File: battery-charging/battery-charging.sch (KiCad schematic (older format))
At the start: 20 parts, among them J101 USB_B_Micro, J102 BAT-, J103 BAT+, U101 TC4056A, U102 MT3608

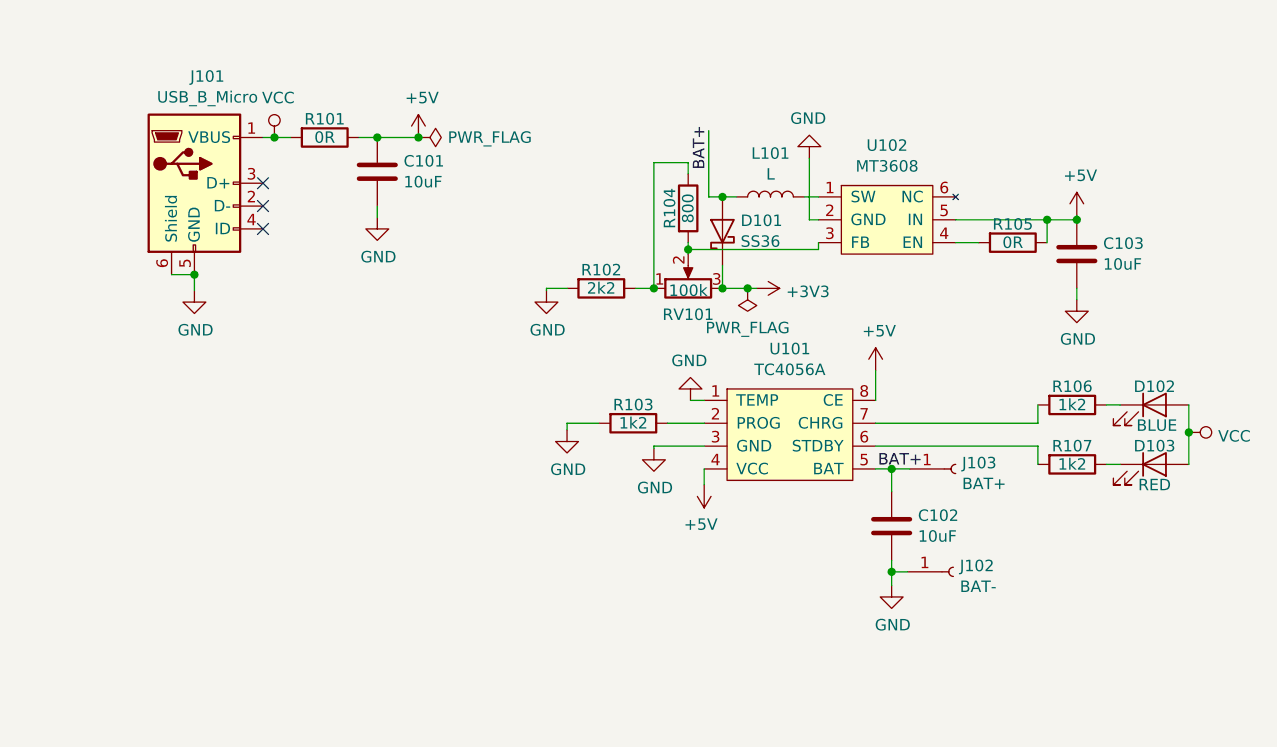
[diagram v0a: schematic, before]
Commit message: added C167321 usb c
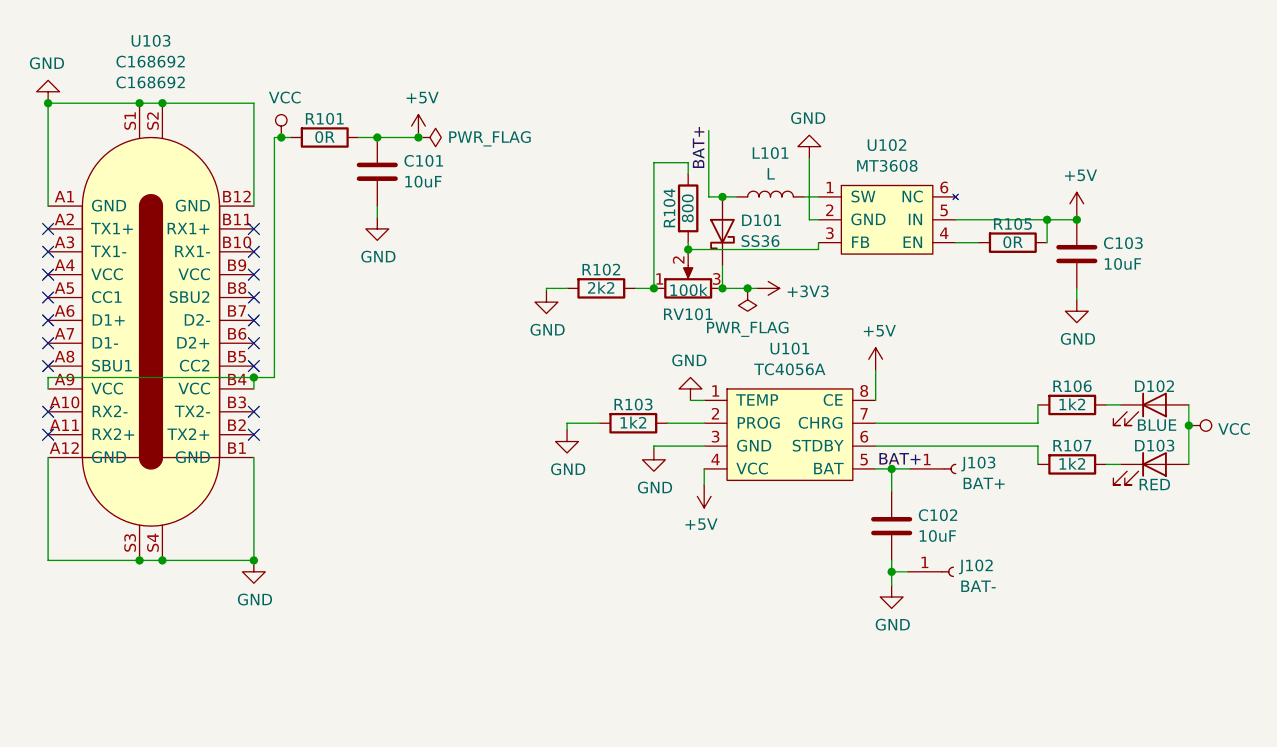
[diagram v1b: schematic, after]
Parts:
- removed J101: USB_B_Micro, Connector_USB:USB_Micro-B_Molex_47346-0001, symbol Connector:USB_B_Micro
- added U103: C168692, water-lib:C168692, symbol water-lib:C168692
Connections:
- net GND: now also U103.A1 (GND), U103.A12 (GND), U103.B1 (GND), U103.B12 (GND), U103.S1, U103.S2, U103.S3, U103.S4
- net VCC: now also U103.A9 (VCC), U103.B4 (VCC)
- no-connect marks 3 -> 18
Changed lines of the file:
@@
 EESchema Schematic File Version 4
+LIBS:battery-charging-cache
 EELAYER 30 0
 EELAYER END
@@
 $EndDescr
 $Comp
-L Connector:USB_B_Micro J101
-U 1 1 5DB449B5
-P 1580 1770
-F 0 "J101" H 1637 2237 50  0000 C CNN
-F 1 "USB_B_Micro" H 1637 2146 50  0000 C CNN
-F 2 "Connector_USB:USB_Micro-B_Molex_47346-0001" H 1730 1720 50  0001 C CNN
-F 3 "~" H 1730 1720 50  0001 C CNN
-	1    1580 1770
-	1    0    0    -1
-$EndComp
-$Comp
 L battery:TC4056A U101
 U 1 1 5DB4BCFC
@@
 	1    0    0    -1
 $EndComp
-NoConn ~ 1880 1770
-NoConn ~ 1880 1870
-Wire Wire Line
-	1480 2170 1580 2170
-Wire Wire Line
-	1580 2170 1580 2240
-Connection ~ 1580 2170
-$Comp
-L power:GND #PWR0101
-U 1 1 5DB4CB22
-P 1580 2240
-F 0 "#PWR0101" H 1580 1990 50  0001 C CNN
-F 1 "GND" H 1585 2067 50  0000 C CNN
-F 2 "" H 1580 2240 50  0001 C CNN
-F 3 "" H 1580 2240 50  0001 C CNN
-	1    1580 2240
-	1    0    0    -1
-$EndComp
 $Comp
 L Device:R R101
@@
 	0    1    1    0
 $EndComp
-Wire Wire Line
-	1880 1570 1930 1570
 $Comp
 L Device:C C101
@@
 	1    0    0    -1
 $EndComp
-NoConn ~ 1880 1970
 $Comp
 L power:GND #PWR0103
@@
 L power:VCC #PWR0110
 U 1 1 5DB57939
-P 1930 1570
-F 0 "#PWR0110" H 1930 1420 50  0001 C CNN
-F 1 "VCC" H 1947 1743 50  0000 C CNN
-F 2 "" H 1930 1570 50  0001 C CNN
-F 3 "" H 1930 1570 50  0001 C CNN
-	1    1930 1570
-	1    0    0    -1
-$EndComp
-Connection ~ 1930 1570
-Wire Wire Line
-	1930 1570 2000 1570
+P 1960 1570
+F 0 "#PWR0110" H 1960 1420 50  0001 C CNN
+F 1 "VCC" H 1977 1743 50  0000 C CNN
+F 2 "" H 1960 1570 50  0001 C CNN
+F 3 "" H 1960 1570 50  0001 C CNN
+	1    1960 1570
+	1    0    0    -1
+$EndComp
+Wire Wire Line
+	1930 1570 1960 1570
 $Comp
 L power:VCC #PWR0111
 U 1 1 5DB58014
-P 5930 2860
-F 0 "#PWR0111" H 5930 2710 50  0001 C CNN
-F 1 "VCC" V 5947 2988 50  0000 L CNN
-F 2 "" H 5930 2860 50  0001 C CNN
-F 3 "" H 5930 2860 50  0001 C CNN
-	1    5930 2860
+P 5930 2830
+F 0 "#PWR0111" H 5930 2680 50  0001 C CNN
+F 1 "VCC" V 5947 2958 50  0000 L CNN
+F 2 "" H 5930 2830 50  0001 C CNN
+F 3 "" H 5930 2830 50  0001 C CNN
+	1    5930 2830
 	0    1    1    0
 $EndComp
@@
 	1    0    0    -1
 $EndComp
-Wire Wire Line
-	5930 2740 5930 2860
-Connection ~ 5930 2860
-Wire Wire Line
-	5930 2860 5930 3000
 Wire Wire Line
 	5630 2740 5570 2740
@@
 $EndComp
 Connection ~ 2560 1570
+$Comp
+L water-lib:C168692 U103
+U 1 1 5DEF8B80
+P 1390 2370
+F 0 "U103" H 1390 3591 50  0000 C CNN
+F 1 "C168692" H 1390 3500 50  0000 C CNN
+F 2 "water-lib:C168692" H 1240 2370 50  0001 C CNN
+F 3 "https://datasheet.lcsc.com/szlcsc/1811141426_Jing-Extension-of-the-Electronic-Co-C168692_C168692.pdf" H 1240 2370 50  0001 C CNN
+F 4 "C168692" H 1390 3409 50  0000 C CNN "LCSC"
+	1    1390 2370
+	1    0    0    -1
+$EndComp
+Wire Wire Line
+	940  1870 940  1420
+Wire Wire Line
+	940  1420 1340 1420
+Wire Wire Line
+	1840 1420 1840 1870
+Connection ~ 1340 1420
+Wire Wire Line
+	1340 1420 1440 1420
+Connection ~ 1440 1420
+Wire Wire Line
+	1440 1420 1840 1420
+Wire Wire Line
+	940  2670 940  2620
+Wire Wire Line
+	940  2620 1840 2620
+Wire Wire Line
+	1840 2620 1840 2670
+Wire Wire Line
+	1930 1570 1930 2620
+Wire Wire Line
+	1930 2620 1840 2620
+Connection ~ 1840 2620
+Wire Wire Line
+	940  2970 940  3420
+Wire Wire Line
+	940  3420 1340 3420
+Wire Wire Line
+	1840 3420 1840 2970
+Connection ~ 1340 3420
+Wire Wire Line
+	1340 3420 1440 3420
+Connection ~ 1440 3420
+Wire Wire Line
+	1440 3420 1840 3420
+NoConn ~ 940  1970
+NoConn ~ 940  2070
+NoConn ~ 940  2170
+NoConn ~ 940  2270
+NoConn ~ 940  2370
+NoConn ~ 940  2470
+NoConn ~ 940  2570
+NoConn ~ 940  2770
+NoConn ~ 940  2870
+NoConn ~ 1840 2870
+NoConn ~ 1840 2770
+NoConn ~ 1840 2570
+NoConn ~ 1840 2470
+NoConn ~ 1840 2370
+NoConn ~ 1840 2270
+NoConn ~ 1840 2170
+NoConn ~ 1840 2070
+NoConn ~ 1840 1970
+$Comp
+L power:GND #PWR0101
+U 1 1 5DF1FDAC
+P 1840 3420
+F 0 "#PWR0101" H 1840 3170 50  0001 C CNN
+F 1 "GND" H 1845 3247 50  0000 C CNN
+F 2 "" H 1840 3420 50  0001 C CNN
+F 3 "" H 1840 3420 50  0001 C CNN
+	1    1840 3420
+	1    0    0    -1
+$EndComp
+Connection ~ 1840 3420
+$Comp
+L power:GND #PWR0114
+U 1 1 5DF2074A
+P 940 1420
+F 0 "#PWR0114" H 940 1170 50  0001 C CNN
+F 1 "GND" H 945 1247 50  0000 C CNN
+F 2 "" H 940 1420 50  0001 C CNN
+F 3 "" H 940 1420 50  0001 C CNN
+	1    940  1420
+	-1   0    0    1
+$EndComp
+Connection ~ 940  1420
+Connection ~ 1960 1570
+Wire Wire Line
+	1960 1570 2000 1570
+Wire Wire Line
+	5930 2740 5930 2830
+Connection ~ 5930 2830
+Wire Wire Line
+	5930 2830 5930 3000
 $EndSCHEMATC

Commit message: battery changing urb c
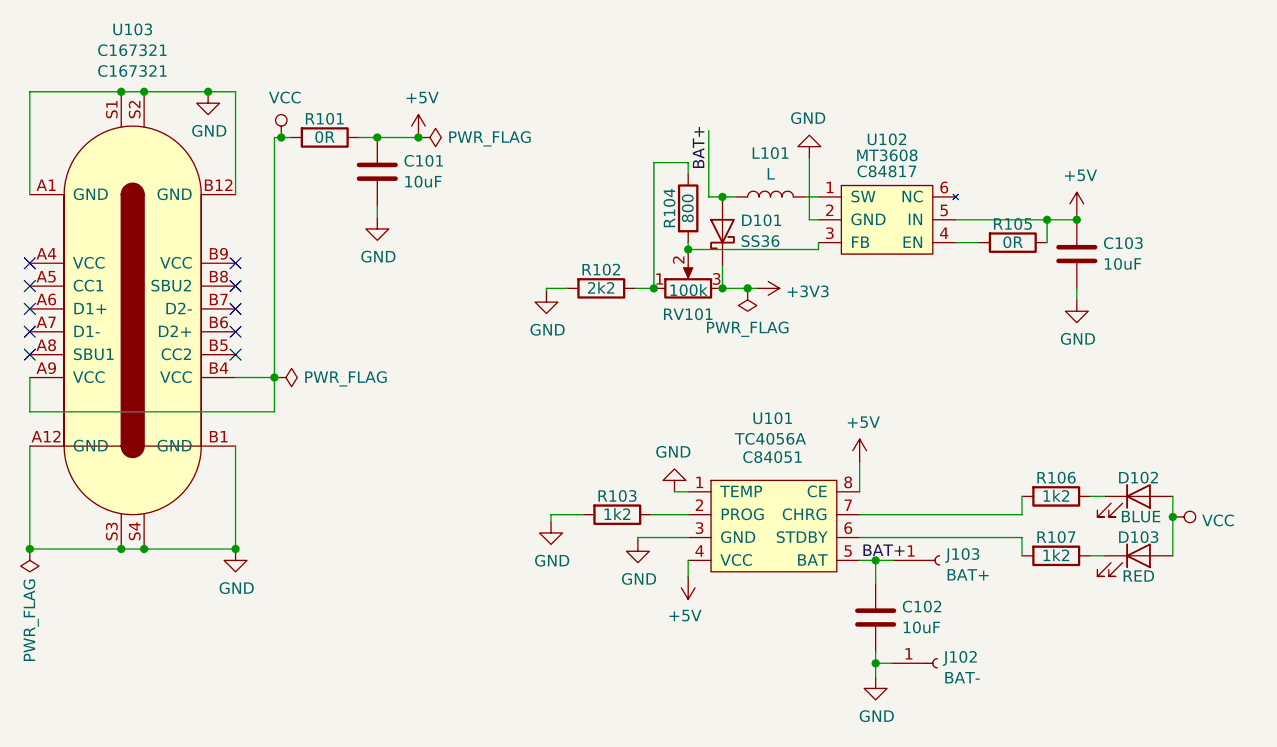
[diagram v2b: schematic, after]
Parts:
- removed U103: C168692, water-lib:C168692, symbol water-lib:C168692
- added U103: C167321, water-lib:C167321, symbol water-lib:C167321
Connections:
- net GND: now also U103.A1 (GND), U103.A12 (GND), U103.B1 (GND), U103.B12 (GND), U103.S1, U103.S2, U103.S3, U103.S4
- net VCC: now also U103.A9 (VCC), U103.B4 (VCC)
- no-connect marks 18 -> 10
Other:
- moved on the sheet: C102, D102, D103, J102, J103, R103, R106, R107, U101
